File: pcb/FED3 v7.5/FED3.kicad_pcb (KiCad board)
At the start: 4 copper layers, 108 x 50 mm, 93 parts, among them IC1 MC74VHC1GT125, IC2 TB6612FNG, IC4 RTC PCF8523T, J1 Conn_02x03_Odd_Even, J6 USB4105-GF-A, Q2 DMP2035U-7, SW1 Sw, SW2 SPST_TACT-KMR2, U1 ATSAMD21G18A, U2 MIC5504-3.3, U3 MCP73834-xxxx, X1 ClockXtal, X2 uXtal, X4 microsd, X5 B2B-PH-K-S

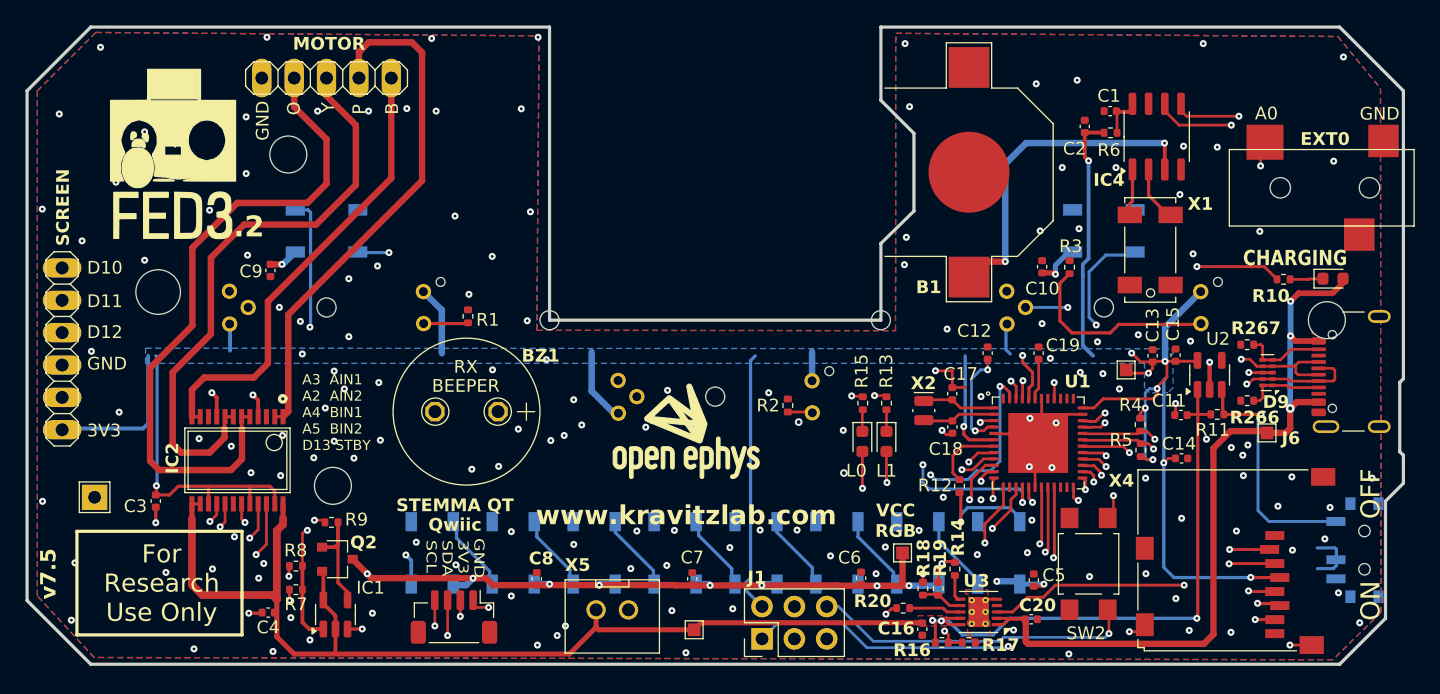
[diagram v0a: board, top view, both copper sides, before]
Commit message: FED3 v.7.5 - 1ºs ficheiros de progução
- adicionada header para opção VTherm = Vbat
- optimização para BOM: variedade-vs-quantidade
- optimização de power-planes
- gerados ficheiros produção para 1ª avaliação; há lá erros reconhecidos
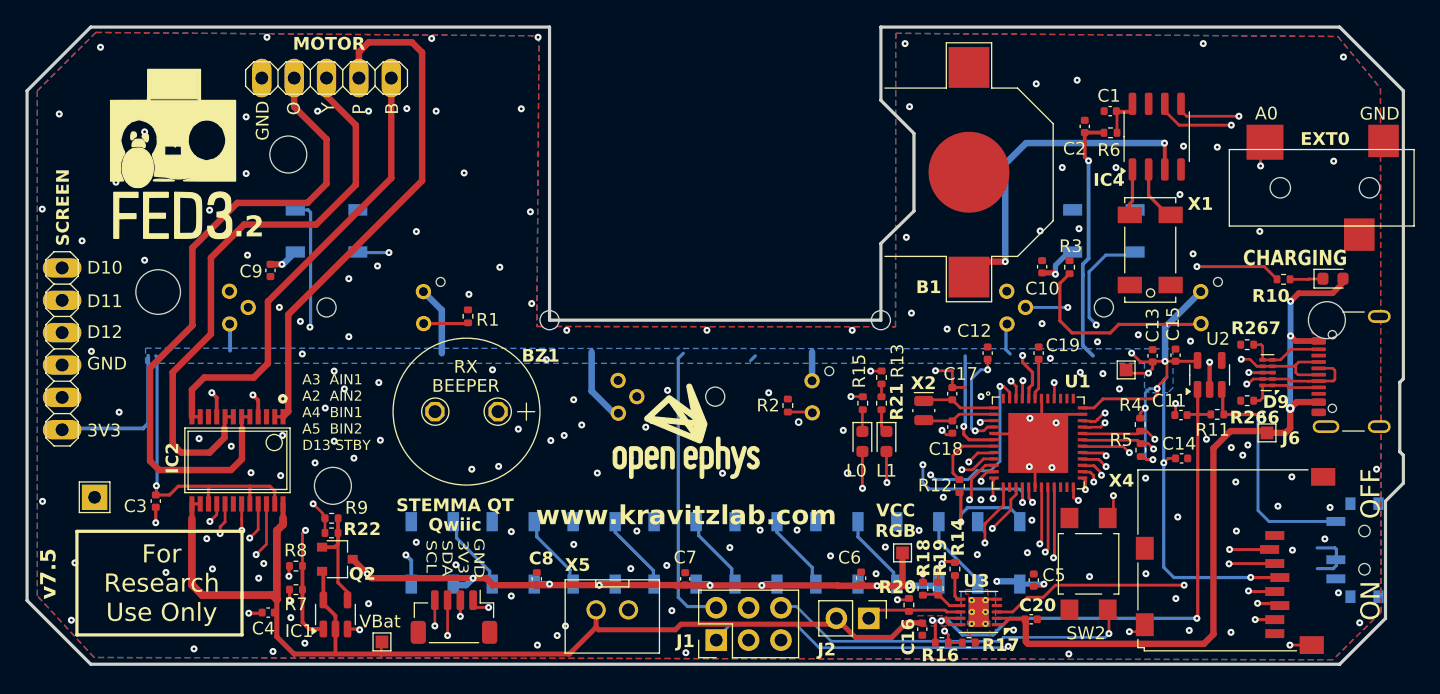
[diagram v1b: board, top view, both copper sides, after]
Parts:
- removed @HOLE1: , 
- added ?: , , F.Cu at (196.5, 103.0)
- added J2: Conn_01x02_Odd_Even, Connector_PinHeader_2.54mm:PinHeader_1x02_P2.54mm_Vertical, F.Cu at (160.6, 126.4)
- added R21: 1k, Resistor_SMD:R_0402_1005Metric, F.Cu at (161.6, 109.5)
- added R22: 100k 0.1%, Resistor_SMD:R_0402_1005Metric, F.Cu at (118.4, 119.7)
- R10: value 1k -> 4k7
- R13: value 2k2 -> 1.27k
- R9: value 34k -> 100k 0.1%
- moved TP3 24.5 mm to (122.3, 128.2)
- moved J1 3.59 mm to (148.6, 128.1)
- moved R13 2.06 mm to (161.6, 107.5)
- moved C7 0.55 mm to (146.2, 123.3)
- moved R20 0.51 mm to (163.7, 125.3), turned to 90 degrees
- moved R9 0.32 mm to (118.4, 118.5)
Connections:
- R13 pad 1: Net-(L1-K) -> Net-(R13-Pad1)
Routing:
- net /Controller Stage/~{RESET}: track 52.8 -> 56.4 mm
- net Net-(J2-Pin_1): track 3.96 -> 7.51 mm
- net /Controller Stage/SWDIO: track 40.4 -> 43.9 mm
- net /Controller Stage/SWCLK: track 44.7 -> 48.2 mm
- net +3V3: track 226.6 -> 229.3 mm
- net VBat: track 137.0 -> 138.7 mm
- net GND: track 41.5 -> 43.1 mm, vias 153 -> 157
- net Net-(R13-Pad1): track 0.00 -> 1.00 mm
- net A4: track 68.0 -> 67.2 mm
- net D13: track 84.0 -> 84.5 mm

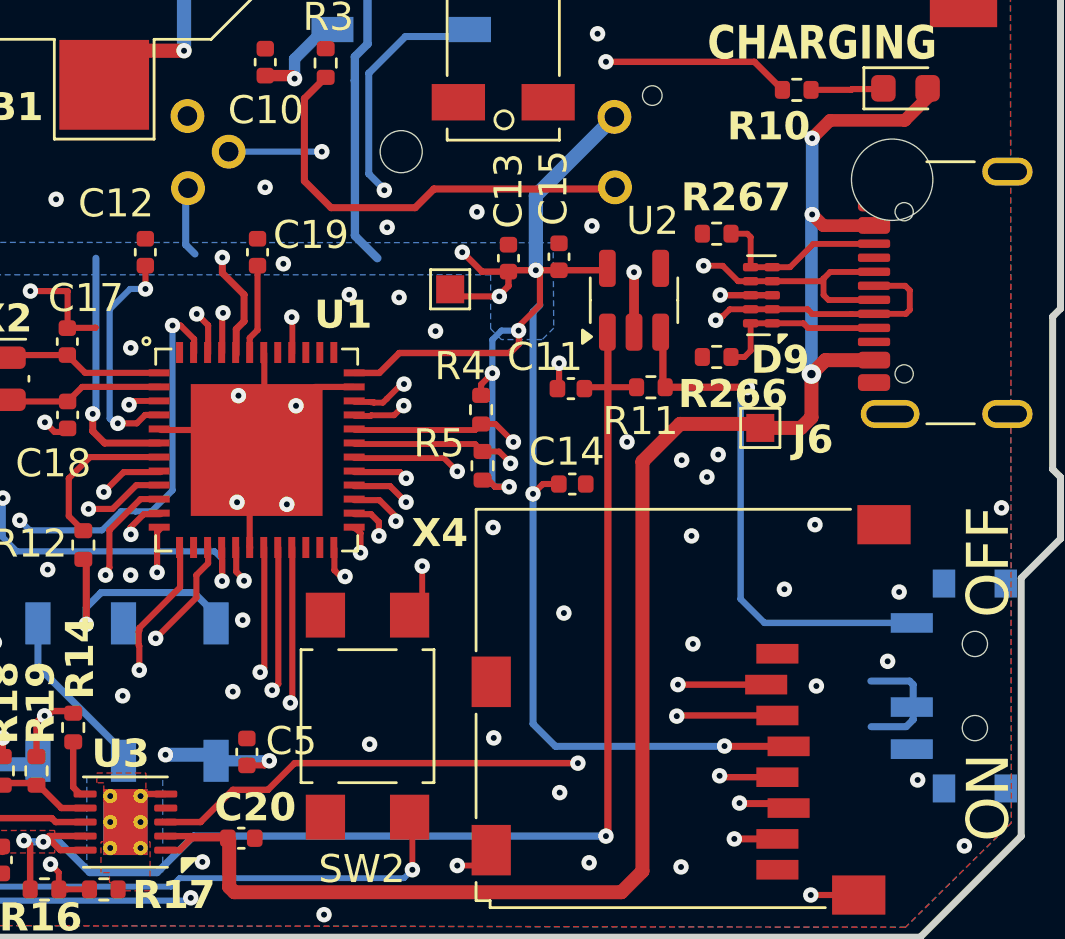
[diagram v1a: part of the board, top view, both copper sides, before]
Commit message: FED3 v.7.5 - 2ºs ficheiros produção
- corrigidas posições de silks de alguns componentes
- modificados Denominators de alguns componentes
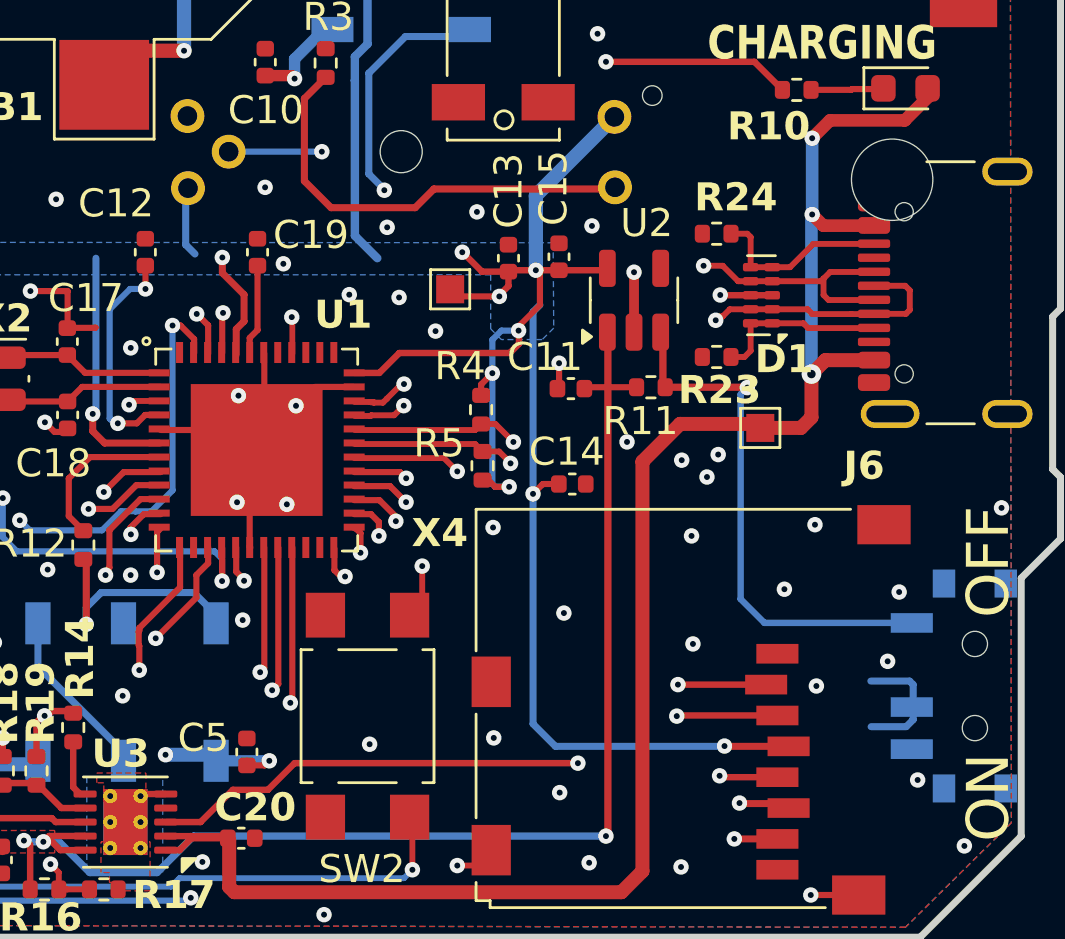
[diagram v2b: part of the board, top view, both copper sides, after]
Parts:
- renumbered D9 to D1, R266 to R23, R267 to R24
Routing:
- net GND: track 43.1 -> 43.0 mm, vias 157 -> 156
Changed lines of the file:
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@@
 	(net 97 "unconnected-(U3-STAT2-Pad4)")
 	(net 98 "Net-(R13-Pad1)")
+	(net 99 "unconnected-(AUX_I2C0-Pin_5-Pad5)")
+	(net 100 "unconnected-(AUX_I2C0-Pin_5-Pad5)_1")
 	(footprint "Button_Switch_SMD:SW_SPST_TL3305B"
 		(locked yes)
@@
 		(descr "Resistor SMD 0402 (1005 Metric), square (rectangular) end terminal, IPC-7351 nominal, (Body size source: IPC-SM-782 page 72, https://www.pcb-3d.com/wordpress/wp-content/uploads/ipc-sm-782a_amendment_1_and_2.pdf), generated with kicad-footprint-generator")
 		(tags "resistor")
-		(property "Reference" "R267"
+		(property "Reference" "R24"
 			(at -0.6858 1.2954 0)
 			(unlocked yes)
@@
 	)
 	(footprint ""
+		(locked yes)
 		(layer "F.Cu")
 		(at 196.5011 103.0036)
@@
 			)
 		)
+		(attr through_hole board_only)
 		(pad "" np_thru_hole circle
 			(at 0 0)
@@
 		(descr "USON-10 2.5x1.0mm_ Pitch 0.5mm http://www.ti.com/lit/ds/symlink/tpd4e02b04.pdf")
 		(tags "USON-10 2.5x1.0mm Pitch 0.5mm")
-		(property "Reference" "D9"
-			(at -0.6644 -2.302 0)
+		(property "Reference" "D1"
+			(at -0.8078 -2.2788 0)
 			(unlocked yes)
 			(layer "F.SilkS")
@@
 		(descr "Resistor SMD 0402 (1005 Metric), square (rectangular) end terminal, IPC-7351 nominal, (Body size source: IPC-SM-782 page 72, https://www.pcb-3d.com/wordpress/wp-content/uploads/ipc-sm-782a_amendment_1_and_2.pdf), generated with kicad-footprint-generator")
 		(tags "resistor")
-		(property "Reference" "R266"
-			(at -0.5842 -1.3208 0)
+		(property "Reference" "R23"
+			(at -0.104 -1.1784 0)
 			(unlocked yes)
 			(layer "F.SilkS")
@@
 			)
 		)
-		(property "Description" "Generic connector, single row, 01x04, script generated (kicad-library-utils/schlib/autogen/connector/)"
+		(property "Description" "Generic connector, single row, 01x05, script generated (kicad-library-utils/schlib/autogen/connector/)"
 			(at 0 0 180)
 			(unlocked yes)
@@
 			(pintype "passive")
 		)
-		(pad "MP" smd roundrect
+		(pad "5" smd roundrect
 			(at -2.8 -1.2 180)
 			(size 1.2 1.8)
+			(property pad_prop_heatsink)
 			(layers "F.Cu" "F.Mask" "F.Paste")
 			(roundrect_rratio 0.208333)
+			(net 99 "unconnected-(AUX_I2C0-Pin_5-Pad5)")
+			(pinfunction "Pin_5")
+			(pintype "passive+no_connect")
 		)
-		(pad "MP" smd roundrect
+		(pad "5" smd roundrect
 			(at 2.8 -1.2 180)
 			(size 1.2 1.8)
 			(layers "F.Cu" "F.Mask" "F.Paste")
 			(roundrect_rratio 0.208333)
+			(net 100 "unconnected-(AUX_I2C0-Pin_5-Pad5)_1")
+			(pinfunction "Pin_5")
+			(pintype "passive+no_connect")
 		)
 		(embedded_fonts no)
@@
 		(tags "USB C Type-C Receptacle SMD USB 2.0 16P 16C USB4105-15-A USB4105-15-A-060 USB4105-15-A-120 USB4105-GF-A USB4105-GF-A-060 USB4105-GF-A-120")
 		(property "Reference" "J6"
-			(at -5.2344 -5.8592 0)
+			(at -6.1664 -4.0342 0)
 			(unlocked yes)
 			(layer "F.SilkS")
@@
 		(tags "capacitor")
 		(property "Reference" "C5"
-			(at 0.3878 1.5822 0)
+			(at 0.5 -1.55 0)
 			(layer "F.SilkS")
 			(effects
@@
 		(tags "SOT TO_SOT_SMD")
 		(property "Reference" "U2"
-			(at 2.8298 0.66 0)
+			(at 2.75 0.45 0)
 			(layer "F.SilkS")
 			(effects
@@
 	)
 	(segment
-		(start 173 121.25)
-		(end 173.04 121.29)
-		(width 0.22)
-		(layer "F.Cu")
-		(net 1)
-	)
-	(segment
 		(start 166 122.3408)
 		(end 166 123.49)
@@
 	)
 	(via
-		(at 173 121.25)
-		(size 0.55)
-		(drill 0.21)
-		(layers "F.Cu" "B.Cu")
-		(net 1)
-	)
-	(via
 		(at 115.95 103.1)
 		(size 0.55)
@@
 	)
 	(segment
-		(start 189.7792 106.0704)
-		(end 189.738 106.1116)
-		(width 0.21)
-		(layer "In1.Cu")
-		(net 71)
-	)
-	(segment
-		(start 189.738 107.6452)
-		(end 187.6332 109.75)
+		(start 179.575 110.625)
+		(end 179.275 110.325)
 		(width 0.21)
 		(layer "In1.Cu")
@@
 	)
 	(segment
-		(start 185.7818 110.625)
+		(start 186.7582 110.625)
 		(end 179.575 110.625)
 		(width 0.21)
@@
 	)
 	(segment
-		(start 186.6568 109.75)
-		(end 185.7818 110.625)
+		(start 189.7792 106.0704)
+		(end 189.738 106.1116)
 		(width 0.21)
 		(layer "In1.Cu")
@@
 	)
 	(segment
-		(start 187.6332 109.75)
-		(end 186.6568 109.75)
+		(start 179.138177 110.325)
+		(end 179.100448 110.287271)
 		(width 0.21)
 		(layer "In1.Cu")
@@
 	)
 	(segment
-		(start 179.575 110.625)
-		(end 179.275 110.325)
+		(start 189.738 107.6452)
+		(end 186.7582 110.625)
 		(width 0.21)
 		(layer "In1.Cu")
@@
 	)
 	(segment
-		(start 179.138177 110.325)
-		(end 179.100448 110.287271)
-		(width 0.21)
-		(layer "In1.Cu")
-		(net 71)
-	)
-	(segment
 		(start 195.0384 107.7912)
 		(end 195.9166 107.7912)
@@
 	)
 	(segment
-		(start 187.993152 110.2)
-		(end 186.8432 110.2)
+		(start 179.642781 111.057219)
+		(end 179.09131 111.057219)
 		(width 0.21)
 		(layer "In1.Cu")
@@
 	)
 	(segment
-		(start 185.9882 111.055)
+		(start 187.138152 111.055)
 		(end 179.645 111.055)
 		(width 0.21)
@@
 	)
 	(segment
-		(start 190.179793 108.013359)
-		(end 187.993152 110.2)
-		(width 0.21)
-		(layer "In1.Cu")
-		(net 73)
-	)
-	(segment
-		(start 179.645 111.055)
-		(end 179.642781 111.057219)
-		(width 0.21)
-		(layer "In1.Cu")
-		(net 73)
-	)
-	(segment
 		(start 190.211771 108.013359)
 		(end 190.179793 108.013359)
@@
 	)
 	(segment
-		(start 179.642781 111.057219)
-		(end 179.09131 111.057219)
+		(start 179.645 111.055)
+		(end 179.642781 111.057219)
 		(width 0.21)
 		(layer "In1.Cu")
@@
 	)
 	(segment
-		(start 186.8432 110.2)
-		(end 185.9882 111.055)
+		(start 190.179793 108.013359)
+		(end 187.138152 111.055)
 		(width 0.21)
 		(layer "In1.Cu")
